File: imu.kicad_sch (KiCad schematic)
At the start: 5 parts, among them IC5 LSM6DSV16BXTR

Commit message: group parts on pcb
replace footprints
update can setup
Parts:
- C1, C2: footprint (none) -> Capacitor_SMD:C_0603_1608Metric
- IC5: footprint LSM6DSV16BXTR -> SamacSys_Parts:LSM6DSV16BXTR
- R1, R2: footprint (none) -> Resistor_SMD:R_0603_1608Metric
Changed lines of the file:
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@@
 			)
 		)
-		(property "Footprint" ""
+		(property "Footprint" "Resistor_SMD:R_0603_1608Metric"
 			(at 135.89 72.39 0)
 			(effects
@@
 			)
 		)
-		(property "Footprint" ""
+		(property "Footprint" "Capacitor_SMD:C_0603_1608Metric"
 			(at 167.64 104.14 0)
 			(effects
@@
 			)
 		)
-		(property "Footprint" ""
+		(property "Footprint" "Resistor_SMD:R_0603_1608Metric"
 			(at 135.89 64.77 0)
 			(effects
@@
 			)
 		)
-		(property "Footprint" ""
+		(property "Footprint" "Capacitor_SMD:C_0603_1608Metric"
 			(at 147.32 130.81 0)
 			(effects
@@
 			)
 		)
-		(property "Footprint" "LSM6DSV16BXTR"
+		(property "Footprint" "SamacSys_Parts:LSM6DSV16BXTR"
 			(at 161.29 178.74 0)
 			(effects

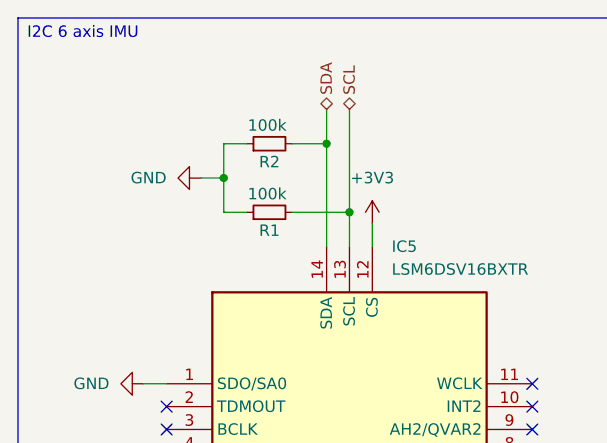
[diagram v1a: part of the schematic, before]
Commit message: fix i2c pull up
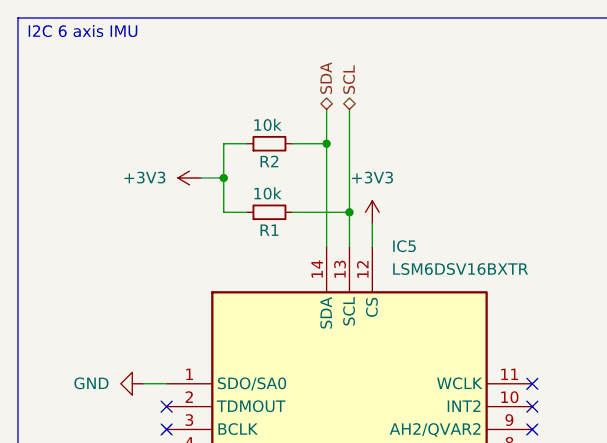
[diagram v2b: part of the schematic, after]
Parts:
- R1, R2: value 100k -> 10k
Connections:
- net +3V3: now also R1.1, R2.1
- net GND: no longer R1.1, R2.1
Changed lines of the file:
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@@
 			)
 		)
-		(property "Value" "100k"
+		(property "Value" "10k"
 			(at 135.636 70.358 90)
 			(effects
@@
 				(path "/be608b80-d1f2-4edd-b7a6-2b7cddd9f44f/272dd5a9-e141-4f8d-9723-e5b5520e8b08"
 					(reference "R1")
+					(unit 1)
+				)
+			)
+		)
+	)
+	(symbol
+		(lib_id "power:+3V3")
+		(at 128.27 68.58 90)
+		(unit 1)
+		(exclude_from_sim no)
+		(in_bom yes)
+		(on_board yes)
+		(dnp no)
+		(fields_autoplaced yes)
+		(property "Reference" "#PWR067"
+			(at 132.08 68.58 0)
+			(effects
+				(font
+					(size 1.27 1.27)
+				)
+				(hide yes)
+			)
+		)
+		(property "Value" "+3V3"
+			(at 124.46 68.5799 90)
+			(effects
+				(font
+					(size 1.27 1.27)
+				)
+				(justify left)
+			)
+		)
+		(property "Footprint" ""
+			(at 128.27 68.58 0)
+			(effects
+				(font
+					(size 1.27 1.27)
+				)
+				(hide yes)
+			)
+		)
+		(property "Datasheet" ""
+			(at 128.27 68.58 0)
+			(effects
+				(font
+					(size 1.27 1.27)
+				)
+				(hide yes)
+			)
+		)
+		(property "Description" "Power symbol creates a global label with name \"+3V3\""
+			(at 128.27 68.58 0)
+			(effects
+				(font
+					(size 1.27 1.27)
+				)
+				(hide yes)
+			)
+		)
+		(pin "1"
+		)
+		(instances
+			(project "glr-pcb-all2can"
+				(path "/be608b80-d1f2-4edd-b7a6-2b7cddd9f44f/272dd5a9-e141-4f8d-9723-e5b5520e8b08"
+					(reference "#PWR067")
 					(unit 1)
 				)
@@
 	)
 	(symbol
-		(lib_id "power:GND")
-		(at 128.27 68.58 270)
-		(unit 1)
-		(exclude_from_sim no)
-		(in_bom yes)
-		(on_board yes)
-		(dnp no)
-		(fields_autoplaced yes)
-		(property "Reference" "#PWR067"
-			(at 121.92 68.58 0)
-			(effects
-				(font
-					(size 1.27 1.27)
-				)
-				(hide yes)
-			)
-		)
-		(property "Value" "GND"
-			(at 124.46 68.5799 90)
-			(effects
-				(font
-					(size 1.27 1.27)
-				)
-				(justify right)
-			)
-		)
-		(property "Footprint" ""
-			(at 128.27 68.58 0)
-			(effects
-				(font
-					(size 1.27 1.27)
-				)
-				(hide yes)
-			)
-		)
-		(property "Datasheet" ""
-			(at 128.27 68.58 0)
-			(effects
-				(font
-					(size 1.27 1.27)
-				)
-				(hide yes)
-			)
-		)
-		(property "Description" "Power symbol creates a global label with name \"GND\" , ground"
-			(at 128.27 68.58 0)
-			(effects
-				(font
-					(size 1.27 1.27)
-				)
-				(hide yes)
-			)
-		)
-		(pin "1"
-		)
-		(instances
-			(project "glr-pcb-all2can"
-				(path "/be608b80-d1f2-4edd-b7a6-2b7cddd9f44f/272dd5a9-e141-4f8d-9723-e5b5520e8b08"
-					(reference "#PWR067")
-					(unit 1)
-				)
-			)
-		)
-	)
-	(symbol
 		(lib_id "Device:R_Small")
 		(at 135.89 64.77 90)
@@
 			)
 		)
-		(property "Value" "100k"
+		(property "Value" "10k"
 			(at 135.636 62.738 90)
 			(effects

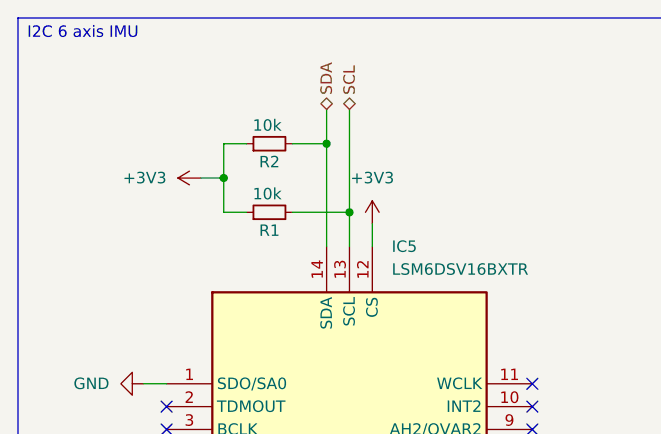
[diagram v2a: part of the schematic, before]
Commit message: reorder more
move pullup i2c in schematic
make power passing routes thicker
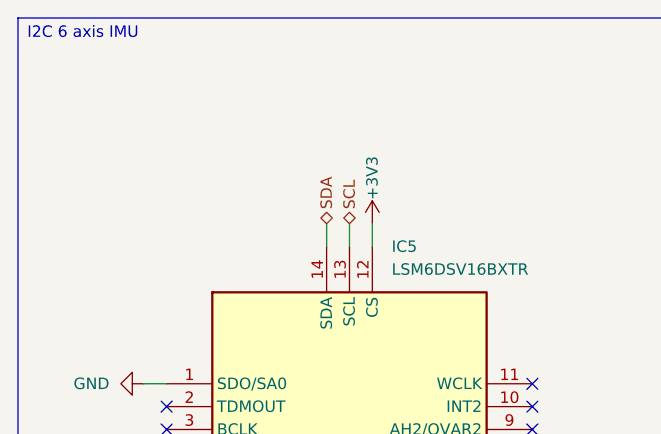
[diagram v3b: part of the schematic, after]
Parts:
- removed R1, R2: 10k, Resistor_SMD:R_0603_1608Metric, symbol Device:R_Small
